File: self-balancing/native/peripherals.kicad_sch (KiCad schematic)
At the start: 15 parts, among them U10 SN74LVC2G17DBVR, U3 ICM-42688-P

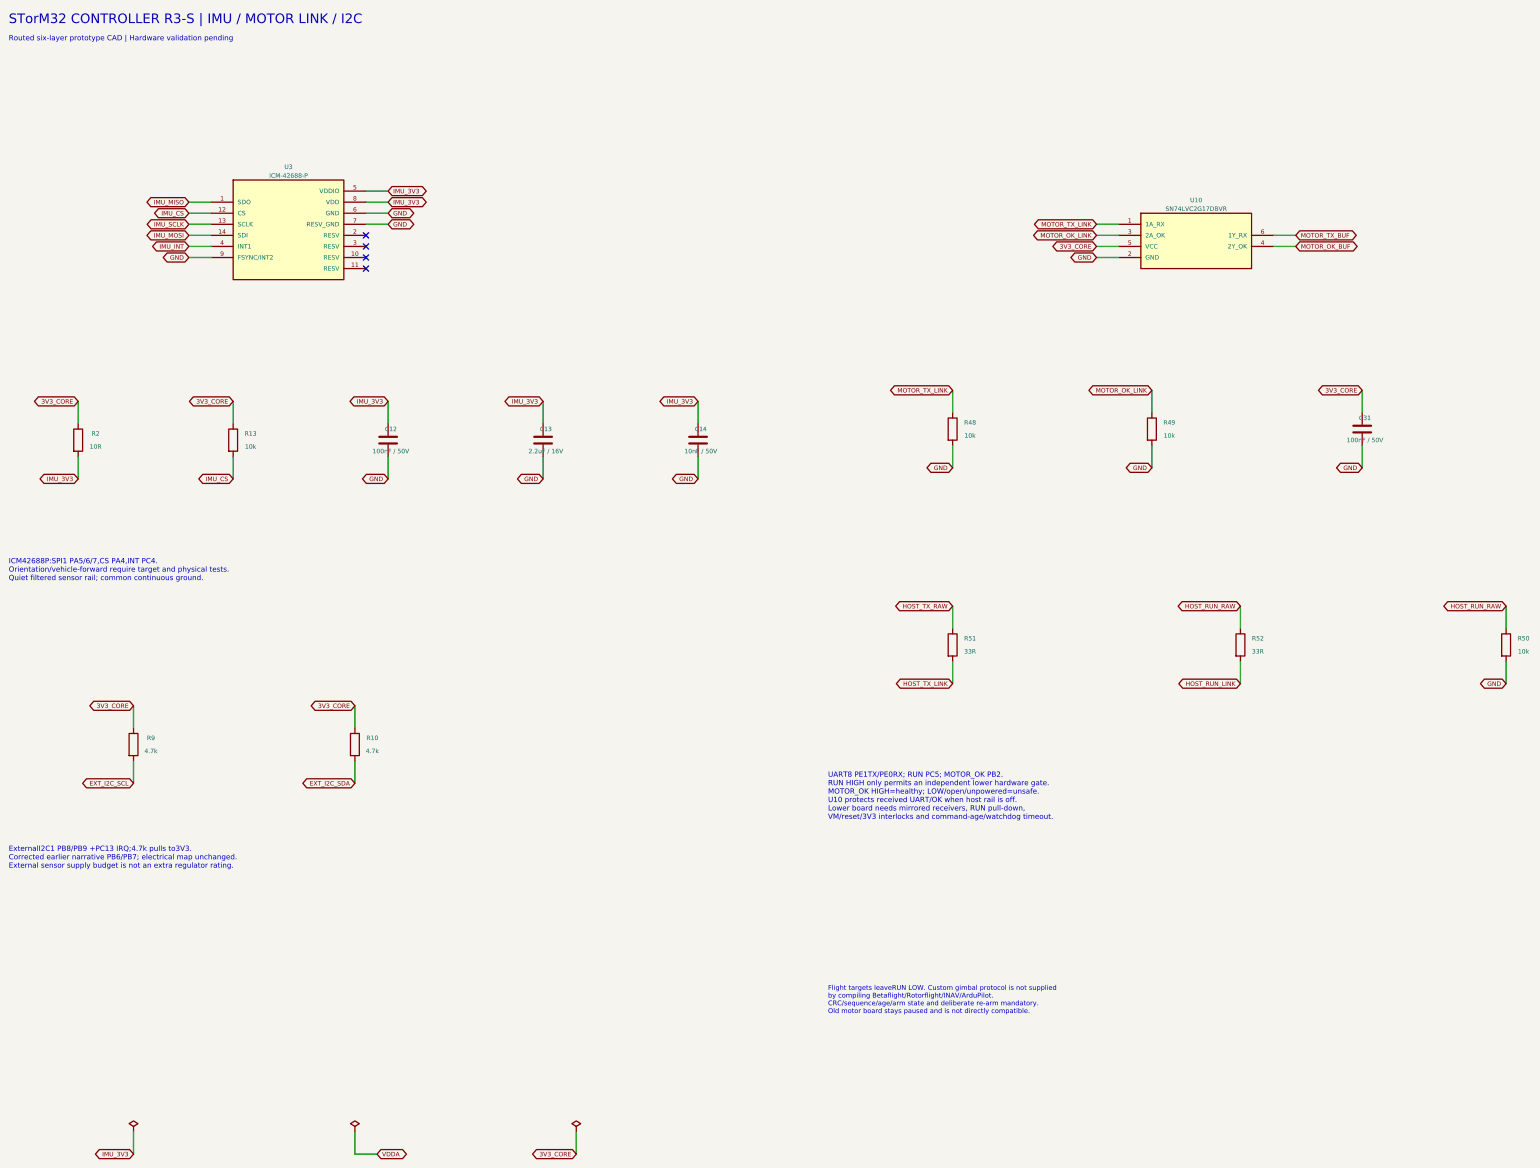
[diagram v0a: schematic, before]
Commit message: Improve H743 schematic readability with wired functional groups
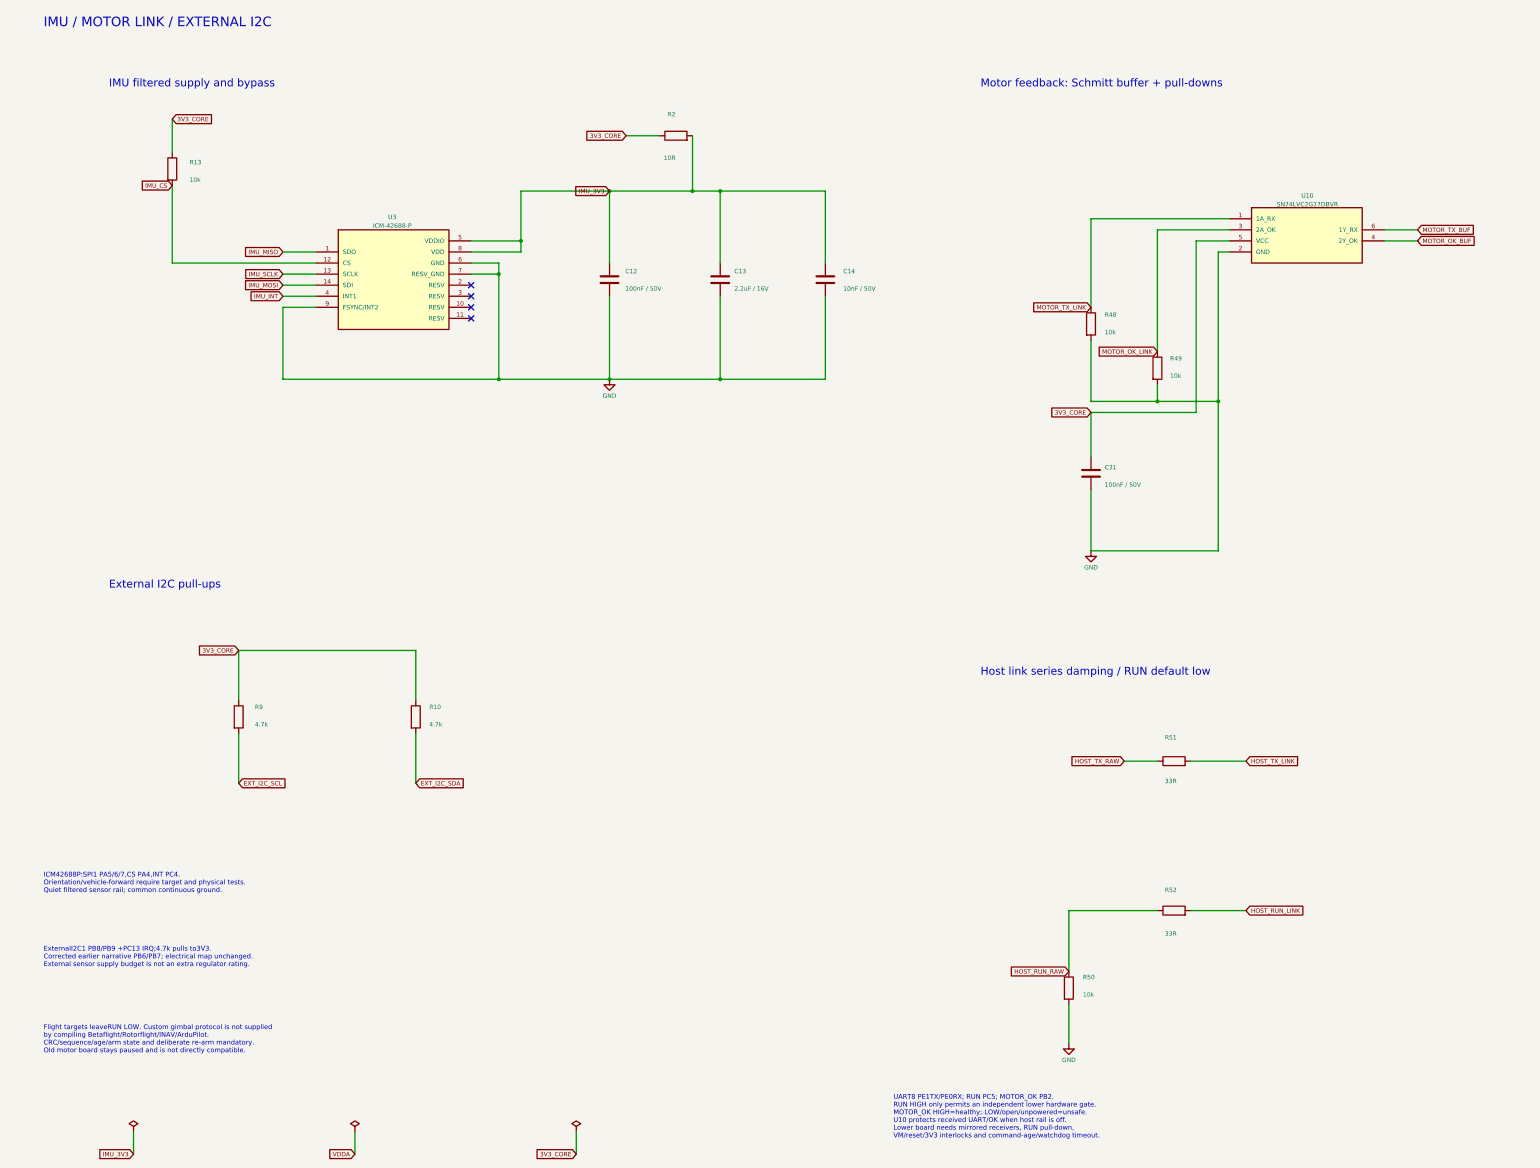
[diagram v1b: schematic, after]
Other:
- note added: "External I2C pull-ups"
- note added: "Host link series damping / RUN default low"
- note added: "IMU / MOTOR LINK / EXTERNAL I2C"
- note added: "IMU filtered supply and bypass"
- note added: "Motor feedback: Schmitt buffer + pull-downs"
- note removed: "Routed six-layer prototype CAD | Hardware validation pending"
- note removed: "STorM32 CONTROLLER R3-S | IMU / MOTOR LINK / I2C"
- moved on the sheet: C12, C13, C14, C31, R10, R13, R2, R48, R49, R50, R51, R52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
